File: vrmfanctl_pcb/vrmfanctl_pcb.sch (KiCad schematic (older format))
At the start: 6 parts, among them J1 SATA Power Male, J2 Pin socket L-shape, J3 Pin socket L-shape, U1 ATtiny85-20PU

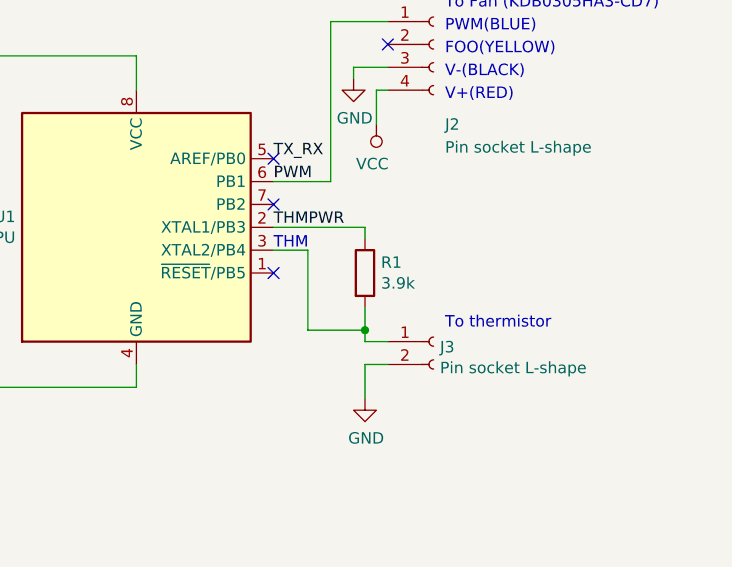
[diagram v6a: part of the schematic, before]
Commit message: update thermistor config. change R1 resistor to 4.7K.
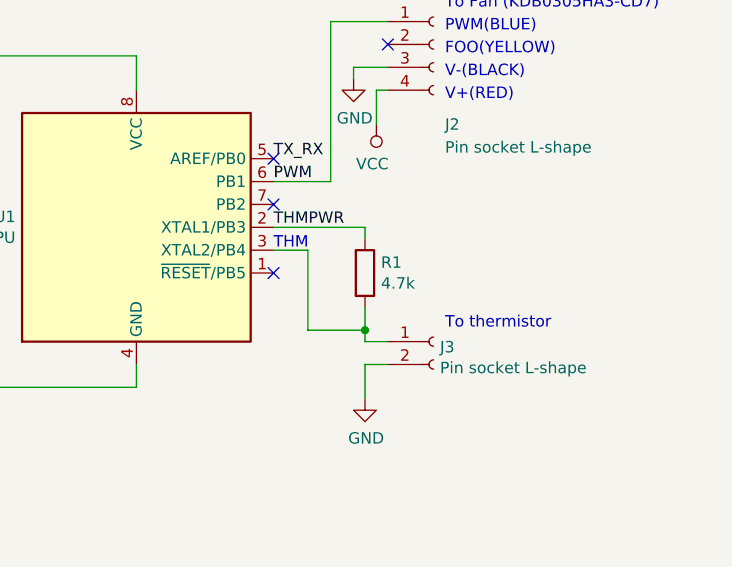
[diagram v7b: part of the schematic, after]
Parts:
- R1: value 3.9k -> 4.7k
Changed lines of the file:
@@
 EESchema Schematic File Version 4
 LIBS:vrmfanctl_pcb-cache
-EELAYER 30 0
+EELAYER 26 0
 EELAYER END
 $Descr A4 11693 8268
@@
 P 5500 2300
 F 0 "R1" H 5570 2346 50  0000 L CNN
-F 1 "3.9k" H 5570 2255 50  0000 L CNN
+F 1 "4.7k" H 5570 2255 50  0000 L CNN
 F 2 "Resistor_THT:R_Axial_DIN0204_L3.6mm_D1.6mm_P5.08mm_Horizontal" V 5430 2300 50  0001 C CNN
 F 3 "~" H 5500 2300 50  0001 C CNN
